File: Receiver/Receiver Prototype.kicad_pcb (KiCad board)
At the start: 4 copper layers, 69 parts, among them J1 Conn_01x02_Socket, J10 Conn_01x01, J11 Conn_Coaxial, J12 Conn_Coaxial, J2 Conn_01x03, J3 Conn_01x01, J4 Conn_Coaxial, J5 Conn_01x01, J6 Conn_01x02, J7 Conn_Coaxial, J8 Conn_Coaxial, J9 Conn_01x01, U1 OPA3692ID, U2 AD8692ARZ, U3 OPA692IDBVR, U5 AD607ARSZ

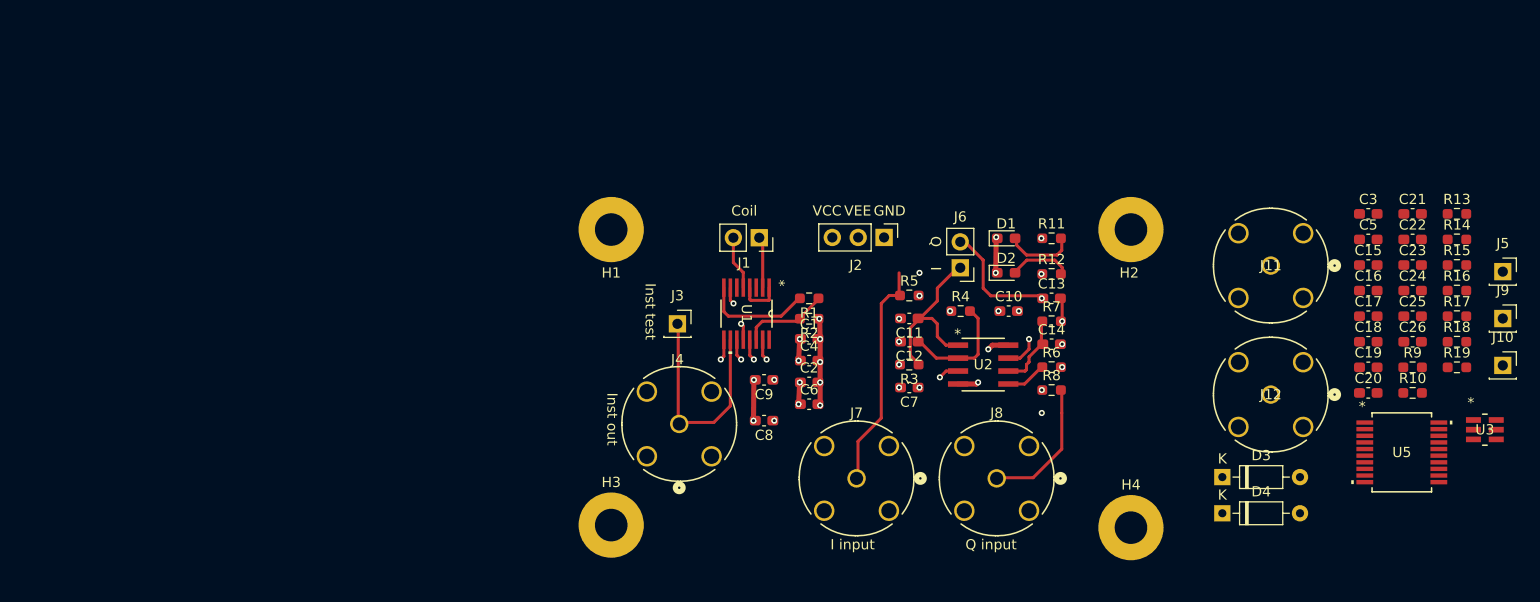
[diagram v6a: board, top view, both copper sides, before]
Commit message: Receiver schematic complete. ERC not passed due to issues with GND
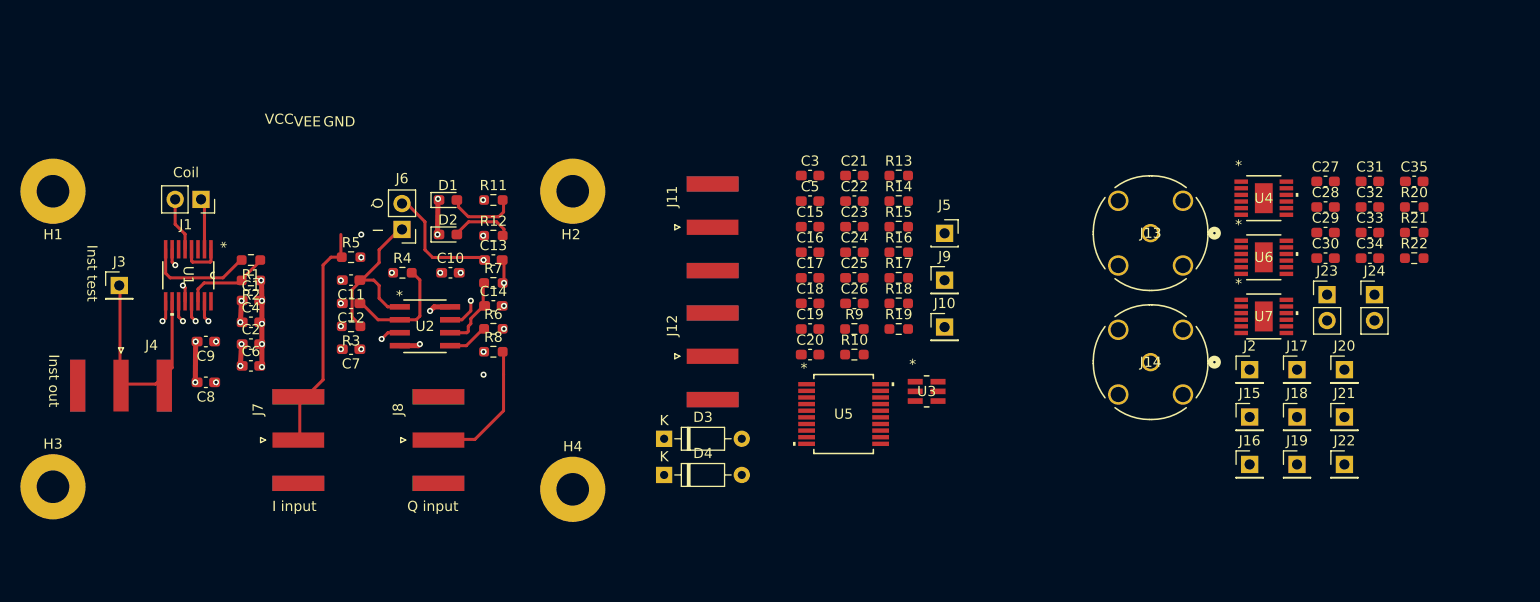
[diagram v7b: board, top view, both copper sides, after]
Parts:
- added C27: 4.7u, Capacitor_SMD:C_0603_1608Metric_Pad1.08x0.95mm_HandSolder, F.Cu at (213.6, 65.8)
- added C28: 10u, Capacitor_SMD:C_0603_1608Metric_Pad1.08x0.95mm_HandSolder, F.Cu at (213.6, 68.3)
- added C29: 0.47u, Capacitor_SMD:C_0603_1608Metric_Pad1.08x0.95mm_HandSolder, F.Cu at (213.6, 70.8)
- added C30: C, Capacitor_SMD:C_0603_1608Metric_Pad1.08x0.95mm_HandSolder, F.Cu at (213.6, 73.3)
- added C31: 0.47u, Capacitor_SMD:C_0603_1608Metric_Pad1.08x0.95mm_HandSolder, F.Cu at (217.9, 65.8)
- added C32: C, Capacitor_SMD:C_0603_1608Metric_Pad1.08x0.95mm_HandSolder, F.Cu at (217.9, 68.3)
- added C33: 4.7u, Capacitor_SMD:C_0603_1608Metric_Pad1.08x0.95mm_HandSolder, F.Cu at (217.9, 70.8)
- added C34: 0.47u, Capacitor_SMD:C_0603_1608Metric_Pad1.08x0.95mm_HandSolder, F.Cu at (217.9, 73.3)
- added C35: 10u, Capacitor_SMD:C_0603_1608Metric_Pad1.08x0.95mm_HandSolder, F.Cu at (222.3, 65.8)
- added J13: Conn_Coaxial, BNC 112404:CONN_112404_AMP, F.Cu at (196.4, 70.9)
- added J14: Conn_Coaxial, BNC 112404:CONN_112404_AMP, F.Cu at (196.4, 83.5)
- added J15: Conn_01x01, Connector_PinHeader_2.54mm:PinHeader_1x01_P2.54mm_Vertical, F.Cu at (206.1, 88.9)
- added J16: Conn_01x01, Connector_PinHeader_2.54mm:PinHeader_1x01_P2.54mm_Vertical, F.Cu at (206.1, 93.5)
- added J17: Conn_01x01, Connector_PinHeader_2.54mm:PinHeader_1x01_P2.54mm_Vertical, F.Cu at (210.8, 84.2)
- added J18: Conn_01x01, Connector_PinHeader_2.54mm:PinHeader_1x01_P2.54mm_Vertical, F.Cu at (210.8, 88.9)
- added J19: Conn_01x01, Connector_PinHeader_2.54mm:PinHeader_1x01_P2.54mm_Vertical, F.Cu at (210.8, 93.5)
- added J20: Conn_01x01, Connector_PinHeader_2.54mm:PinHeader_1x01_P2.54mm_Vertical, F.Cu at (215.4, 84.2)
- added J21: Conn_01x01, Connector_PinHeader_2.54mm:PinHeader_1x01_P2.54mm_Vertical, F.Cu at (215.4, 88.9)
- added J22: Conn_01x01, Connector_PinHeader_2.54mm:PinHeader_1x01_P2.54mm_Vertical, F.Cu at (215.4, 93.5)
- added J23: Conn_01x02, Connector_PinHeader_2.54mm:PinHeader_1x02_P2.54mm_Vertical, F.Cu at (213.7, 76.9)
- added J24: Conn_01x02, Connector_PinHeader_2.54mm:PinHeader_1x02_P2.54mm_Vertical, F.Cu at (218.4, 76.9)
- added R20: 49.9k, Resistor_SMD:R_0603_1608Metric_Pad0.98x0.95mm_HandSolder, F.Cu at (222.3, 68.3)
- added R21: 33.2k, Resistor_SMD:R_0603_1608Metric_Pad0.98x0.95mm_HandSolder, F.Cu at (222.3, 70.8)
- added R22: 49.9k, Resistor_SMD:R_0603_1608Metric_Pad0.98x0.95mm_HandSolder, F.Cu at (222.3, 73.3)
- added U4: LT3045EMSE-PBF, LT3045 MSOP:MSOP12_MSE_ADI, F.Cu at (207.5, 67.4)
- added U6: LT3094EMSE-PBF, LT3094 MSOP:05-08-1666_ADI, F.Cu at (207.5, 73.2)
- added U7: LT3045EMSE-PBF, LT3045 MSOP:MSOP12_MSE_ADI, F.Cu at (207.5, 79.0)
- J10, J3, J9: footprint Connector_PinSocket_2.54mm:PinSocket_1x01_P2.54mm_Vertical -> Connector_PinHeader_2.54mm:PinHeader_1x01_P2.54mm_Vertical
- J11, J12, J4, J7, J8: footprint BNC 112404:CONN_112404_AMP -> Connector_Coaxial:SMA_Amphenol_132289_EdgeMount
- J2: value Conn_01x03 -> Conn_01x01; footprint Connector_PinHeader_2.54mm:PinHeader_1x03_P2.54mm_Vertical -> Connector_PinHeader_2.54mm:PinHeader_1x01_P2.54mm_Vertical
- moved C1 54.9 mm to (108.2, 77.5)
- moved C10 54.9 mm to (127.7, 74.7)
- moved C11 54.9 mm to (118.0, 75.5)
- moved C12 54.9 mm to (118.0, 77.7)
- moved C13 54.9 mm to (131.9, 73.5)
- moved C14 54.9 mm to (131.9, 78.0)
- moved C15 54.9 mm to (163.0, 70.2)
- moved C16 54.9 mm to (163.0, 72.7)
- moved C17 54.9 mm to (163.0, 75.2)
- moved C18 54.9 mm to (163.0, 77.8)
- moved C19 54.9 mm to (163.0, 80.3)
- moved C2 54.9 mm to (108.2, 81.7)
- moved C20 54.9 mm to (163.0, 82.8)
- moved C3 54.9 mm to (163.0, 65.2)
- moved C4 54.9 mm to (108.2, 79.6)
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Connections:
- net /+3V renamed /+3.3_out
- C17 pad 2: Net-(JP1-A) -> Net-(U5-GREF)
- J2 pad 1: GND -> /PWR+
- R16 pad 1: Net-(JP1-A) -> Net-(U5-GREF)
- U5 pad 7: Net-(JP1-B) -> Net-(U5-GREF)
- U5 pad 9: Net-(JP1-A) -> Net-(U5-GREF)

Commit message: Receiver ready for DR2. DRC not passed due to SMA connectors
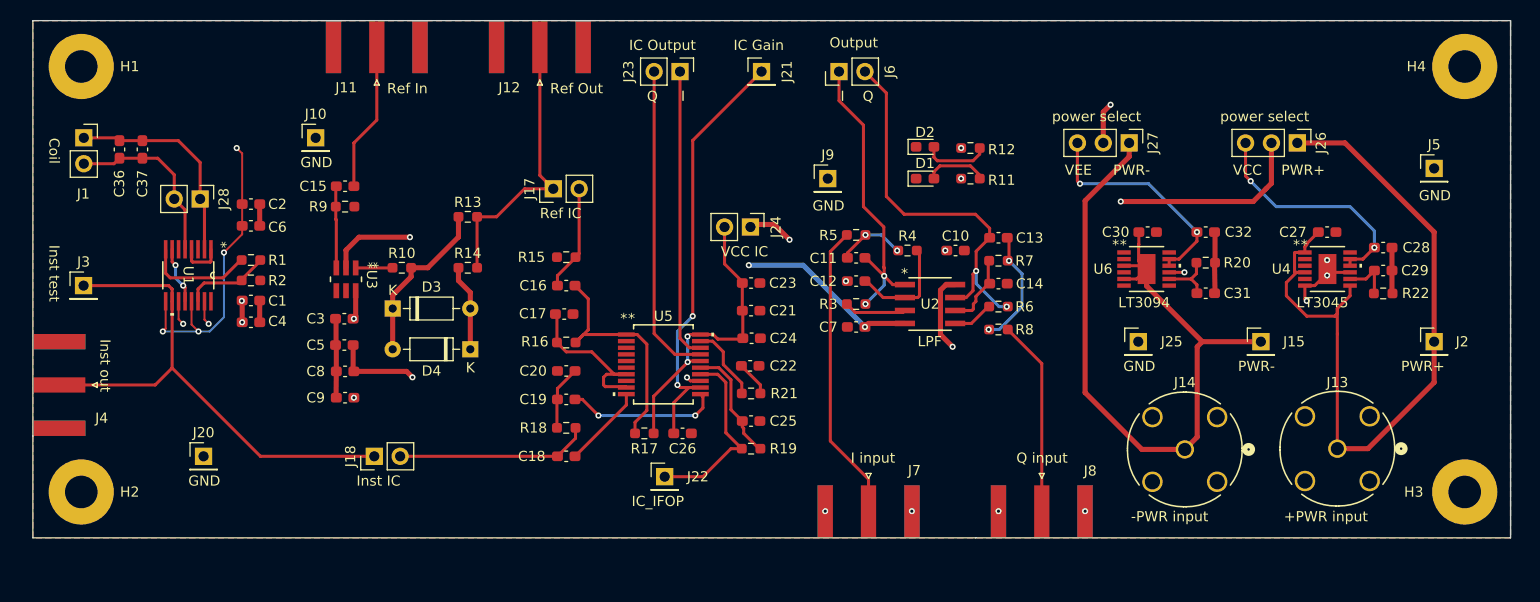
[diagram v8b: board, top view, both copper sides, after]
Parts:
- removed C33: 4.7u, Capacitor_SMD:C_0603_1608Metric_Pad1.08x0.95mm_HandSolder
- removed C34: 0.47u, Capacitor_SMD:C_0603_1608Metric_Pad1.08x0.95mm_HandSolder
- removed C35: 10u, Capacitor_SMD:C_0603_1608Metric_Pad1.08x0.95mm_HandSolder
- removed J16, J19: Conn_01x01, Connector_PinHeader_2.54mm:PinHeader_1x01_P2.54mm_Vertical
- removed U7: LT3045EMSE-PBF, LT3045 MSOP:MSOP12_MSE_ADI
- added C36: C, Capacitor_SMD:C_0603_1608Metric_Pad1.08x0.95mm_HandSolder, F.Cu at (95.2, 62.6)
- added C37: C, Capacitor_SMD:C_0603_1608Metric_Pad1.08x0.95mm_HandSolder, F.Cu at (97.5, 62.6)
- added J25: Conn_01x01, Connector_PinHeader_2.54mm:PinHeader_1x01_P2.54mm_Vertical, F.Cu at (195.2, 81.5)
- added J26: Conn_01x03, Connector_PinHeader_2.54mm:PinHeader_1x03_P2.54mm_Vertical, F.Cu at (210.8, 62.0)
- added J27: Conn_01x03, Connector_PinHeader_2.54mm:PinHeader_1x03_P2.54mm_Vertical, F.Cu at (194.3, 62.0)
- added J28: Conn_01x02, Connector_PinHeader_2.54mm:PinHeader_1x02_P2.54mm_Vertical, F.Cu at (103.2, 67.5)
- C30, C32: value C -> 10u
- C31: value 0.47u -> 4.7u
- J17, J18: value Conn_01x01 -> Conn_01x02; footprint Connector_PinHeader_2.54mm:PinHeader_1x01_P2.54mm_Vertical -> Connector_PinHeader_2.54mm:PinHeader_1x02_P2.54mm_Vertical
- J5: footprint Connector_PinSocket_2.54mm:PinSocket_1x01_P2.54mm_Vertical -> Connector_PinHeader_2.54mm:PinHeader_1x01_P2.54mm_Vertical
- R10, R13, R14: value R -> 100
- R21: value 33.2k -> 1k
- moved H3 138.5 mm to (227.2, 96.2)
- moved J20 112.3 mm to (103.5, 92.8)
- moved H4 96.9 mm to (227.2, 54.5)
- moved J18 90.6 mm to (120.2, 92.8), turned to 90 degrees
- moved J17 75.1 mm to (137.8, 66.5), turned to 90 degrees
- moved J23 67.2 mm to (150.2, 55.0), turned to -90 degrees
- moved R21 67.0 mm to (157.2, 86.6)
- moved J22 66.7 mm to (148.8, 94.8)
- moved J21 66.5 mm to (158.2, 55.0)
- moved J10 64.4 mm to (114.5, 61.5)
- moved J24 61.6 mm to (157.2, 70.2), turned to -90 degrees
- moved J8 59.6 mm to (185.8, 98.1), turned to -90 degrees
- moved U3 58.0 mm to (117.5, 75.4), turned to -90 degrees
- moved H2 56.5 mm to (91.5, 96.2)
- moved J7 56.4 mm to (168.8, 98.1), turned to -90 degrees
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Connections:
- net /+3.3_out renamed /VCC_IC
- C22 pad 1: Net-(U5-FLTR) -> Net-(C22-Pad1)
- C28 pad 1: VCC -> /VCC_In
- C32 pad 1: VEE -> /VEE_In
- D3 pad 2: Net-(D3-A) -> GND
- D4 pad 1: Net-(D3-A) -> GND
- J18 pad 1: VCC -> /Inst_Out
- J20 pad 1: /+3.3V -> GND
- J24 pad 1: /+3.3V -> VCC
- R14 pad 1: Net-(D3-A) -> GND
- R21 pad 1: Net-(U7-SET) -> Net-(U5-FLTR)
- R21 pad 2: GND -> Net-(C22-Pad1)
- U4 pad 10: VCC -> /VCC_In
- U4 pad 11: VCC -> /VCC_In
- U6 pad 10: VEE -> /VEE_In
- U6 pad 11: VEE -> /VEE_In
- U6 pad 13: unconnected-(U6-IN-Pad13) -> /PWR-
- U6 pad 2: /PWR- -> unconnected-(U6-IN-Pad2)
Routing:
- net /PWR+: track 0.00 -> 76.1 mm
- net /PWR-: track 0.00 -> 73.7 mm
- net VEE: track 8.55 -> 69.7 mm, vias 8 -> 10
- net /Inst_Out: track 21.7 -> 70.7 mm
- net /IC_Gain: track 0.00 -> 42.8 mm, vias 0 -> 2
- net /Reference_Out: track 0.00 -> 38.4 mm
- net VCC: track 8.82 -> 41.6 mm, vias 8 -> 11
- net /IC_Q: track 0.00 -> 31.1 mm
- net /VCC_IC: track 0.00 -> 29.8 mm, vias 0 -> 2
- net /IC_I: track 0.00 -> 28.6 mm
- net GND: track 16.3 -> 42.3 mm, vias 15 -> 10
- net Net-(U5-FDIN): track 0.00 -> 23.6 mm
- net /VCC_In: track 0.00 -> 23.3 mm, vias 0 -> 2
- net /VEE_In: track 0.00 -> 22.5 mm, vias 0 -> 2
- net /IC_IFOP: track 0.00 -> 18.7 mm
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- added copper zone on B.Cu, net GND
- added copper zone on F.Cu, net GND
- added copper zone on In1.Cu, net GND
- added copper zone on In2.Cu, net VCC
- added copper zone on In2.Cu, net VEE
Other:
- board outline added: 145 x 50.8 mm
- board text added: "+PWR input"
- board text added: "-PWR input"
- board text added: "IC Gain"
- board text added: "IC Output"
- board text added: "IC_IFOP"
- board text added: "Inst IC"
- board text added: "LPF"
- board text added: "LT3045"
- board text added: "LT3094"
- board text added: "Output"
- board text added: "PWR+"
- board text added: "PWR-"
- board text added: "Ref IC"
- board text added: "Ref In"
- board text added: "Ref Out"
- board text added: "VCC IC"
- board text added: "power select"
